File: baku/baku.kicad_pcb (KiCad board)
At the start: 2 copper layers, 177.8 x 82.6 mm, 67 parts, among them IC1 ESP32-CAM, J1 USB_B_Mini, J10 Conn_01x03, J11 Conn_Coaxial, J12 Conn_Coaxial, J13 Conn_01x05_Male, J14 Conn_01x05_Male, J2 Conn_02x05_Odd_Even, J3 Conn_02x05_Odd_Even, J7 J1B1211CCD, J8 Micro_SD_Card, J9 Conn_01x05_Male, U10 74HC164, U11 PDME1-S5-D3-S, U12 ADP7142AUJZ-2.5, U13 ADP7182AUJZ-2.5, U14 REF5020AD, U15 MAX9632, U16 MAX11169, U17 MCP4801, U18 OP07, U20 ESP32-WROOM-32, U21 74HC164, U22 ULN2003A, U23 ULN2003A, U24 ULN2003A, U25 ULN2003A, U5 Teensy4.1, U6 Pico, U8 AZ1117-3.3, U9 AZ1117-3.3

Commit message: Changes
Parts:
- added C28: CP1_Small, Capacitor_SMD:C_1206_3216Metric, F.Cu at (133.6, 69.5)
- added J4: Conn_02x05_Odd_Even, Connector_PinHeader_2.54mm:PinHeader_2x05_P2.54mm_Vertical, F.Cu at (121.2, 120.0)
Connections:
- U6 pad 36: /pipico/3V3 -> +3V3
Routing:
- net /-2V5: track 145.4 -> 199.0 mm
- net /2V5: track 155.7 -> 200.8 mm
- net /REF: track 98.0 -> 129.4 mm
- net /DAC_LDAC: track 76.8 -> 102.6 mm
- net GND: track 742.3 -> 755.8 mm
- net /VDD3V3: track 86.4 -> 97.6 mm
- net /GNDA: track 194.3 -> 199.5 mm
- net +5V: track 338.2 -> 339.5 mm
- net /A_BUTTON1: track 146.4 -> 147.4 mm
- net /SPI4_MISO: track 159.6 -> 160.6 mm
- net /SPI4_SCLK: track 122.8 -> 123.4 mm

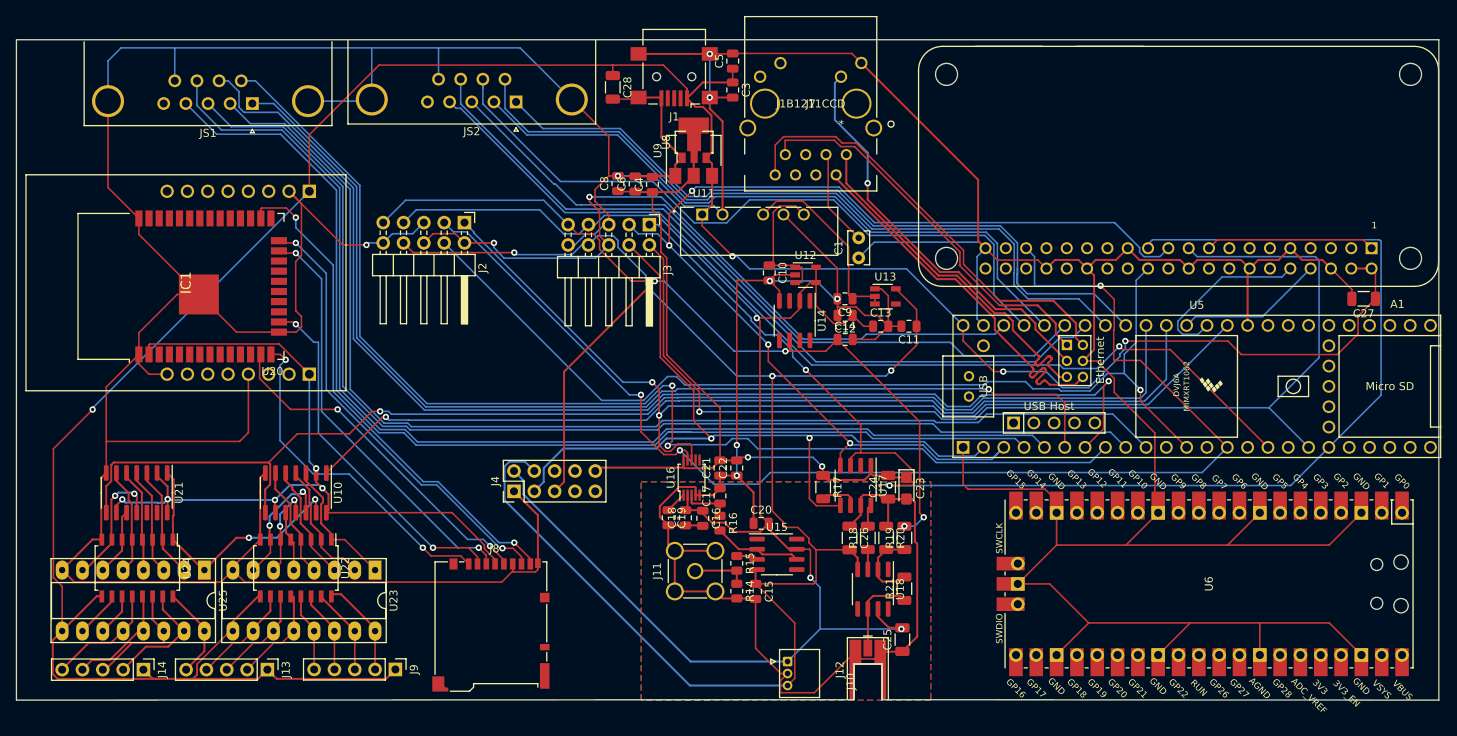
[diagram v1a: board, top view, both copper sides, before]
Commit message: About to remove the onboard adc/dac
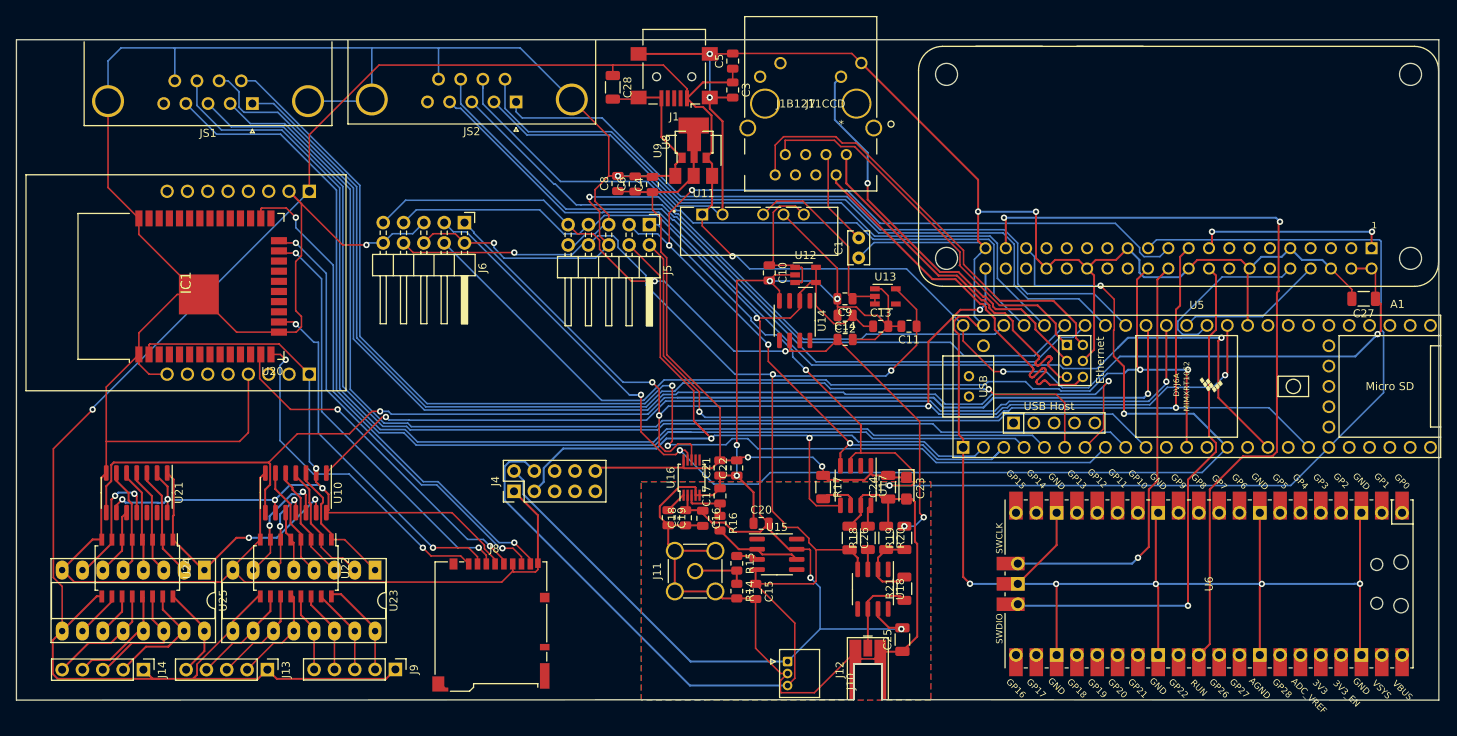
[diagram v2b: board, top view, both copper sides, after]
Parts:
- removed J2, J3: Conn_02x05_Odd_Even, Connector_PinHeader_2.54mm:PinHeader_2x05_P2.54mm_Horizontal
- added J5: Conn_02x05_Odd_Even, Connector_PinHeader_2.54mm:PinHeader_2x05_P2.54mm_Horizontal, F.Cu at (138.2, 86.6)
- added J6: Conn_02x05_Odd_Even, Connector_PinHeader_2.54mm:PinHeader_2x05_P2.54mm_Horizontal, F.Cu at (115.1, 86.4)
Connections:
- net Net-(U6-Pad1) renamed /pipico/GPIO0
- net Net-(U6-Pad10) renamed /pipico/GPIO7
- net Net-(U6-Pad11) renamed /pipico/GPIO8
- net Net-(U6-Pad12) renamed /pipico/GPIO9
- net Net-(U6-Pad14) renamed /pipico/GPIO10
- net Net-(U6-Pad15) renamed /pipico/GPIO11
- net Net-(U6-Pad16) renamed /pipico/GPIO12
- net Net-(U6-Pad17) renamed /pipico/GPIO13
- net Net-(U6-Pad19) renamed /pipico/GPIO14
- net Net-(U6-Pad2) renamed /pipico/GPIO1
- net Net-(U6-Pad20) renamed /pipico/GPIO15
- net Net-(U6-Pad21) renamed /pipico/GPIO16
- net Net-(U6-Pad22) renamed /pipico/GPIO17
- net Net-(U6-Pad24) renamed /pipico/GPIO18
- net Net-(U6-Pad25) renamed /pipico/GPIO19
- net Net-(U6-Pad26) renamed /pipico/GPIO20
- net Net-(U6-Pad27) renamed /pipico/GPIO21
- net Net-(U6-Pad29) renamed /pipico/GPIO22
- net Net-(U6-Pad31) renamed /pipico/GPIO26
- net Net-(U6-Pad32) renamed /pipico/GPIO27
- net Net-(U6-Pad34) renamed /pipico/GPIO28
- net Net-(U6-Pad4) renamed /pipico/GPIO2
- net Net-(U6-Pad5) renamed /pipico/GPIO3
- net Net-(U6-Pad6) renamed /pipico/GPIO4
- net Net-(U6-Pad7) renamed /pipico/GPIO5
- net Net-(U6-Pad9) renamed /pipico/GPIO6
- A1 pad 18: (no net) -> /RPI_GPIO24
- A1 pad 22: (no net) -> /RPI_GPIO25
- A1 pad 37: (no net) -> /RPI_GPIO26
- U6 pad 30: Net-(U6-Pad30) -> /RPI_GPIO26
- U6 pad 36: +3V3 -> /pipico/3V3
- U6 pad 41: Net-(U6-Pad41) -> /RPI_GPIO25
- U6 pad 43: Net-(U6-Pad43) -> /RPI_GPIO24
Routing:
- net /RPI_GPIO26: track 0.00 -> 99.1 mm, vias 0 -> 2
- net /RPI_GPIO24: track 0.00 -> 66.0 mm, vias 0 -> 1
- net /RPI_GPIO25: track 0.00 -> 53.0 mm, vias 0 -> 1
- net /REF: track 129.4 -> 98.0 mm
- net /SPI4_SCLK: track 123.4 -> 148.3 mm, vias 2 -> 5
- net /SPI1_MOSI: track 140.6 -> 123.0 mm, vias 1 -> 2
- net /B_LEFT: track 122.5 -> 128.6 mm
- net /SPI4_CS0: track 123.2 -> 127.4 mm, vias 1 -> 2
- net /SPI4_MISO: track 160.6 -> 164.7 mm, vias 3 -> 4
- net Net-(A1-Pad1): track 21.2 -> 24.3 mm, vias 0 -> 2
- net GND: track 755.8 -> 758.7 mm, vias 4 -> 11
- net /DAC_LDAC: track 102.6 -> 105.2 mm
- net /B_BUTTON2: track 89.4 -> 87.1 mm
- net /B_UP: track 93.8 -> 92.0 mm
- net Net-(R19-Pad1): track 9.91 -> 10.9 mm
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
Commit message: Maybe version 0.1
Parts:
- removed A1: ADA3708, ADA3708:ADA3708_RPI-ZERO
- removed C15, C16, C18, C22: 100nF, Capacitor_SMD:C_0805_2012Metric
- removed C17: 4.7nF, Capacitor_SMD:C_0805_2012Metric
- removed C19, C20, C21: 10uF, Capacitor_SMD:C_0805_2012Metric
- removed C23: CP, Capacitor_Tantalum_SMD:CP_EIA-3216-18_Kemet-A
- removed C24, C25, C26: C, Capacitor_SMD:C_1206_3216Metric
- removed IC1: ESP32-CAM, esp32_3d:ESP32CAM
- removed J11: Conn_Coaxial, Connector_Coaxial:SMA_Amphenol_901-144_Vertical
- removed J12: Conn_Coaxial, Connector_Coaxial:MMCX_Molex_73415-0961_Horizontal_1.0mm-PCB
- removed R14: 50, Resistor_SMD:R_0805_2012Metric
- removed R15: 0, Resistor_SMD:R_0805_2012Metric
- removed R16: 10, Resistor_SMD:R_0805_2012Metric
- removed R17, R19: R, Resistor_SMD:R_1206_3216Metric
- removed R18, R20, R21: 1K, Resistor_SMD:R_1206_3216Metric
- removed U15: MAX9632, Package_SO:SOIC-8_3.9x4.9mm_P1.27mm
- removed U16: MAX11169, Package_SO:MSOP-10_3x3mm_P0.5mm
- removed U17: MCP4801, Package_SO:SOIC-8_3.9x4.9mm_P1.27mm
- removed U18: OP07, Package_SO:SOIC-8_3.9x4.9mm_P1.27mm
- added A2: ADA3708, ADA3708:ADA3708_RPI-ZERO, F.Cu at (204.2, 90.8)
- added J2: Conn_02x05_Odd_Even, Connector_PinHeader_2.54mm:PinHeader_2x05_P2.54mm_Vertical, F.Cu at (160.6, 127.2)
- added J3: Conn_01x03, Connector_PinHeader_2.54mm:PinHeader_1x03_P2.54mm_Vertical, F.Cu at (147.5, 129.5)
- added R1: 10K, Resistor_SMD:R_0805_2012Metric, F.Cu at (86.8, 78.8)
- J4: value Conn_02x05_Odd_Even -> Conn_01x03; footprint Connector_PinHeader_2.54mm:PinHeader_2x05_P2.54mm_Vertical -> Connector_PinHeader_2.54mm:PinHeader_1x03_P2.54mm_Vertical
- moved J4 22.4 mm to (141.5, 129.5), turned to 180 degrees
- moved J10 13.8 mm to (154.2, 127.5), turned to 90 degrees
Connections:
- net +5V renamed /5V
- C4 pad 1: /VDD3V3 -> /3V3
- C6 pad 1: /VDD3V3 -> /3V3
- C8 pad 1: /VDD3V3 -> /3V3
- J4 pad 1: GND -> /2V5
- J4 pad 2: /2V5 -> /GNDA
- J4 pad 3: /DAC_LDAC -> /-2V5
- J6 pad 2: (no net) -> /SPI4_MOSI
- J8 pad 4: +3V3 -> /3V3
- JS1 pad 5: (no net) -> /3V3
- JS2 pad 5: (no net) -> /3V3
- U10 pad 14: +3V3 -> /3V3
- U10 pad 2: +3V3 -> /3V3
- U10 pad 9: +3V3 -> /3V3
- U20 pad 10: (no net) -> /STEP_CLK
- U20 pad 11: (no net) -> /STEP_SIGNAL
- U20 pad 12: (no net) -> /A_SWITCH_COMMON
- U20 pad 2: +3V3 -> /3V3
- U20 pad 25: (no net) -> Net-(R1-Pad2)
- U20 pad 27: (no net) -> /SPI1_MISO
- U20 pad 28: (no net) -> /SPI1_SCLK
- U20 pad 29: (no net) -> /SPI1_MOSI
- U20 pad 3: +3V3 -> /3V3
- U20 pad 30: (no net) -> /DAC_LDAC
- U20 pad 31: (no net) -> /SPI4_MOSI
- U20 pad 33: (no net) -> /SPI4_MISO
- U20 pad 36: (no net) -> /SPI4_SCLK
- U20 pad 37: (no net) -> /SPI4_CS0
- U20 pad 6: (no net) -> /A_LEFT
- U20 pad 7: (no net) -> /A_BUTTON2
- U20 pad 8: (no net) -> /A_UP
- U20 pad 9: (no net) -> /A_DOWN
- U21 pad 14: +3V3 -> /3V3
- U21 pad 2: +3V3 -> /3V3
- U21 pad 9: +3V3 -> /3V3
- U5 pad 13: (no net) -> /SPI4_MOSI
- U6 pad 10: /pipico/GPIO7 -> /SPI4_MISO
- U6 pad 11: /pipico/GPIO8 -> /SPI4_SCLK
- U6 pad 12: /pipico/GPIO9 -> /SPI4_CS0
- U6 pad 14: /pipico/GPIO10 -> /RPI_UART_TX
- U6 pad 15: /pipico/GPIO11 -> /RPI_UART_RX
- U6 pad 16: /pipico/GPIO12 -> /RPI_SPI1_CE0
- U6 pad 17: /pipico/GPIO13 -> /STEP_SIGNAL
- U6 pad 19: /pipico/GPIO14 -> /STEP_CLK
- U6 pad 20: /pipico/GPIO15 -> /A_UP
- U6 pad 21: /pipico/GPIO16 -> /A_DOWN
- U6 pad 22: /pipico/GPIO17 -> /A_LEFT
- U6 pad 24: /pipico/GPIO18 -> /A_BUTTON2
- U6 pad 25: /pipico/GPIO19 -> /A_BUTTON1
- U6 pad 26: /pipico/GPIO20 -> /A_RIGHT
- U6 pad 27: /pipico/GPIO21 -> /A_SWITCH_COMMON
- U6 pad 36: /pipico/3V3 -> /3V3
- U6 pad 4: /pipico/GPIO2 -> /SPI1_MOSI
- U6 pad 5: /pipico/GPIO3 -> /SPI1_MISO
- U6 pad 6: /pipico/GPIO4 -> /SPI1_SCLK
- U6 pad 7: /pipico/GPIO5 -> /DAC_LDAC
- U6 pad 9: /pipico/GPIO6 -> /SPI4_MOSI
- U8 pad 2: /VDD3V3 -> /3V3
- U9 pad 2: /VDD3V3 -> /3V3
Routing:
- net /3V3: track 0.00 -> 360.4 mm, vias 0 -> 10
- net /SPI4_MOSI: track 0.00 -> 238.5 mm, vias 0 -> 6
- net /SPI1_MISO: track 138.8 -> 257.0 mm, vias 4 -> 7
- net +3V3: track 101.2 -> 0.00 mm, vias 5 -> 0
- net /VDD3V3: track 97.6 -> 0.00 mm, vias 2 -> 0
- net /GNDA: track 200.3 -> 103.8 mm, vias 4 -> 2
- net /SPI1_MOSI: track 123.0 -> 209.2 mm, vias 2 -> 4
- net /DAC_LDAC: track 105.2 -> 186.7 mm, vias 2 -> 4
- net /SPI4_SCLK: track 148.3 -> 227.8 mm
- net /STEP_CLK: track 156.1 -> 227.5 mm, vias 2 -> 5
- net /2V5: track 200.8 -> 129.6 mm, vias 3 -> 2
- net /SPI1_SCLK: track 171.9 -> 242.5 mm, vias 2 -> 4
- net /A_BUTTON2: track 141.5 -> 204.5 mm, vias 0 -> 2
- net /STEP_SIGNAL: track 118.3 -> 180.9 mm, vias 2 -> 5
- net /A_LEFT: track 148.0 -> 206.3 mm, vias 0 -> 2
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- added copper zone on B.Cu, net GND
- added copper zone on F.Cu, net GND
- removed copper zone on B.Cu, net /GNDA
- removed copper zone on F.Cu, net /GNDA
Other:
- outline, holes or cut-outs redrawn

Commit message: This is perhaps what was just ordered at JLPCB
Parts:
- added H1: MountingHole_Pad, MountingHole:MountingHole_3mm_Pad_Via, F.Cu at (63.0, 69.2)
- added H2: MountingHole_Pad, MountingHole:MountingHole_3mm_Pad_Via, F.Cu at (132.5, 141.5)
- added H3: MountingHole_Pad, MountingHole:MountingHole_3mm_Pad_Via, F.Cu at (224.5, 69.0)
- added H4: MountingHole_Pad, MountingHole:MountingHole_3mm_Pad_Via, F.Cu at (175.0, 142.0)

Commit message: Starting in on Rev 0.2
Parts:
- C1: value CP -> 0.1uF; footprint Capacitor_THT:C_Rect_L4.0mm_W2.5mm_P2.50mm -> Capacitor_SMD:C_0805_2012Metric
- moved C1 12.7 mm to (169.5, 79.2), turned to 270 degrees
- moved J7 0.36 mm to (162.3, 74.4)
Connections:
- C1 pad 1: GND -> Net-(C1-Pad1)
- C1 pad 2: Net-(C1-Pad2) -> GND
- J7 pad 1: T- -> T+
- J7 pad 2: T+ -> Net-(C1-Pad1)
- J7 pad 3: Net-(C1-Pad2) -> T-
- J7 pad 4: (no net) -> R+
- J7 pad 5: (no net) -> Net-(C1-Pad1)
- J7 pad 6: (no net) -> R-
- J7 pad 7: R+ -> (no net)
- J7 pad 8: R- -> (no net)
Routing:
- net Net-(C1-Pad1): track 0.00 -> 13.7 mm, vias 0 -> 1
- net Net-(C1-Pad2): track 12.1 -> 0.00 mm
- net GND: track 723.9 -> 719.9 mm
- net R-: track 55.5 -> 52.4 mm
- net /IOREF: track 90.9 -> 94.0 mm
- net T+: track 48.7 -> 51.3 mm
- net /SPI4_SCLK: track 227.8 -> 230.4 mm
- net T-: track 45.3 -> 43.1 mm
- net R+: track 49.9 -> 51.8 mm
- net /5V: track 325.0 -> 325.7 mm
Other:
- board text added: "BAKU R0.2"

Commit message: Light trace cleanup
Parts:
- moved C9 0.29 mm to (162.6, 95.6)
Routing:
- net GND: track 719.9 -> 696.8 mm, vias 11 -> 9
- net /A_BUTTON2: track 204.5 -> 219.3 mm
- net /SPI1_SCLK: track 242.5 -> 252.3 mm
- net T+: track 51.3 -> 43.3 mm
- net /REF: track 68.4 -> 74.0 mm
- net /GNDA: track 103.8 -> 98.7 mm
- net Net-(C10-Pad1): track 18.3 -> 14.4 mm
- net /SPI1_MISO: track 257.0 -> 260.8 mm
- net /SPI4_CS0: track 179.8 -> 176.2 mm
- net /DAC_LDAC: track 186.7 -> 189.7 mm
- net /2V5: track 129.6 -> 131.9 mm
- net /SPI4_MOSI: track 238.5 -> 236.2 mm
- net /A_BUTTON1: track 184.2 -> 183.5 mm

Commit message: Not completely sure what these changes are
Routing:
- net /5V: track 325.7 -> 331.2 mm
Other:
- board text added: "-2V5"
- board text added: "2V5"
- board text added: "GND"

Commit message: Fixed plugs for ADC and DAC.. maybe...
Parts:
- J5, J6: footprint Connector_PinHeader_2.54mm:PinHeader_2x05_P2.54mm_Horizontal -> Connector_PinSocket_2.54mm:PinSocket_2x05_P2.54mm_Horizontal
- moved C4 59.8 mm to (163.7, 135.8)
- moved C6 59.4 mm to (160.5, 135.8)
- moved C8 58.9 mm to (156.8, 135.8)
- moved J6 16.1 mm to (102.0, 77.1), turned to 90 degrees
- moved J5 16.0 mm to (125.2, 77.2), turned to 90 degrees
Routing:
- net GND: track 696.8 -> 661.4 mm, vias 9 -> 8
- net /-2V5: track 161.5 -> 128.1 mm, vias 3 -> 2
- net /SPI4_MISO: track 220.9 -> 193.0 mm, vias 5 -> 6
- net /STEP_CLK: track 227.5 -> 212.4 mm, vias 5 -> 6
- net /SPI1_MISO: track 260.8 -> 245.7 mm, vias 7 -> 5
- net /B_UP: track 91.4 -> 102.2 mm
- net /5V: track 331.2 -> 338.4 mm
- net /SPI1_SCLK: track 252.3 -> 258.4 mm
- net /3V3: track 360.4 -> 354.4 mm
- net /B_LEFT: track 131.8 -> 137.7 mm
- net /DAC_LDAC: track 189.7 -> 195.6 mm
- net /B_DOWN: track 83.1 -> 88.3 mm
- net /B_BUTTON2: track 87.2 -> 82.4 mm, vias 0 -> 1
- net /REF: track 74.0 -> 70.0 mm
- net /SPI1_MOSI: track 209.3 -> 212.5 mm
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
